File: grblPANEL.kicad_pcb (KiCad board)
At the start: 4 copper layers, 84 x 55 mm, 152 parts, among them J101 Conn_01x02, J201 2x5x1.27mm, J202 USB_C_Receptacle_USB2.0, J301 Conn_01x02, J401 Conn_01x02, J501 ILI9488, J601 Conn_02x10_Odd_Even, J701 Conn_01x04, J702 Conn_01x04, J703 Conn_01x04, J704 Conn_01x04, Q501 Q_NPN_BEC - S8050, SW201 SW_Push, SW202 SW_Push, U101 MAX17612A, U102 AZ1117-3.3, U201 STM32G0B1CxTxN, U202 USBLC6-2SC6, U301 SN65HVD230, U401 THVD1406, U601 ADP5589, Y201 8MHz

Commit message: some mcu..
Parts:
- removed TP101, TP102, TP103, TP104, TP105, TP301, TP302, TP303, TP304, TP401, TP402, TP403, TP404, TP501, TP502, TP503, TP504, TP505, TP506, TP507, TP601, TP602, TP701, TP702, TP703, TP704, TP705, TP706, TP707, TP708: TestPoint, TestPoint:TestPoint_THTPad_D2.0mm_Drill1.0mm
- moved R502 31.2 mm to (47.4, 170.4)
- moved R503 28.9 mm to (47.4, 168.7), turned to 0 degrees
- moved R603 15.1 mm to (54.8, 153.5), turned to 90 degrees
- moved R602 12.8 mm to (53.2, 153.5), turned to 90 degrees
- moved R601 10.7 mm to (51.6, 153.5), turned to 90 degrees
- moved R604 8.80 mm to (50.0, 153.5), turned to 90 degrees
- moved C206 5.94 mm to (28.2, 170.7)
- moved R201 5.59 mm to (25.5, 160.0), turned to -90 degrees
- moved R206 4.60 mm to (29.9, 170.7), turned to -90 degrees
- moved C203 3.31 mm to (31.5, 163.4), turned to -90 degrees
- moved C202 2.52 mm to (29.9, 163.4)
- moved C501 2.47 mm to (71.9, 148.3), turned to 90 degrees
- moved C204 2.40 mm to (44.9, 164.0)
- moved D201 2.40 mm to (39.9, 171.5)
- moved R203 2.40 mm to (47.4, 165.0)
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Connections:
- net Net-(J501-Pad11) renamed /Display/CONN_SCL
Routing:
- net DISPLAY_SDA: track 0.00 -> 34.5 mm
- net GND: track 49.0 -> 80.5 mm, vias 28 -> 50
- net DISPLAY_SDO: track 0.00 -> 28.1 mm
- net +3V3: track 35.7 -> 57.8 mm, vias 0 -> 1
- net DISPLAY_BACKLIGHT: track 0.00 -> 20.9 mm
- net DISPLAY_RESET: track 0.00 -> 15.1 mm
- net DISPLAY_CS: track 0.00 -> 14.3 mm
- net DISPLAY_D/C: track 0.00 -> 12.1 mm
- net /MCU/HSE_IN: track 0.00 -> 11.6 mm
- net /Display/CONN_SCL: track 0.00 -> 11.1 mm
- net /Display/DIO_GND: track 0.00 -> 10.0 mm
- net /MCU/CONN_SWDIO: track 0.00 -> 9.32 mm, vias 0 -> 1
- net /MCU/CONN_SWCLK: track 0.00 -> 8.90 mm, vias 0 -> 1
- net /MCU/CONN_~{RST}: track 0.00 -> 8.37 mm, vias 0 -> 1
- net /Keypad/KEYPAD_RST: track 0.00 -> 7.55 mm, vias 0 -> 2
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- added copper zone on F.Cu, net +3V3
- added copper zone on F.Cu, net GND

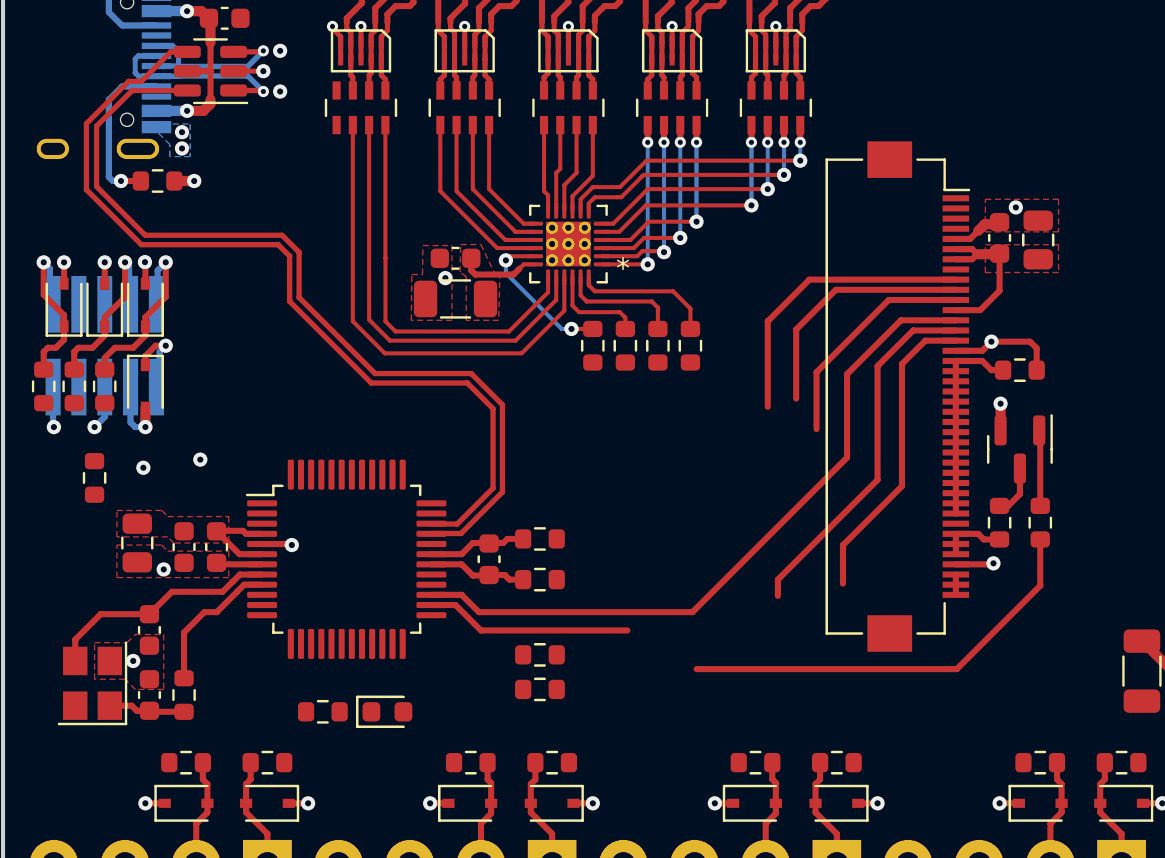
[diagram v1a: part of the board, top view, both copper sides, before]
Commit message: 1st crack at display routing
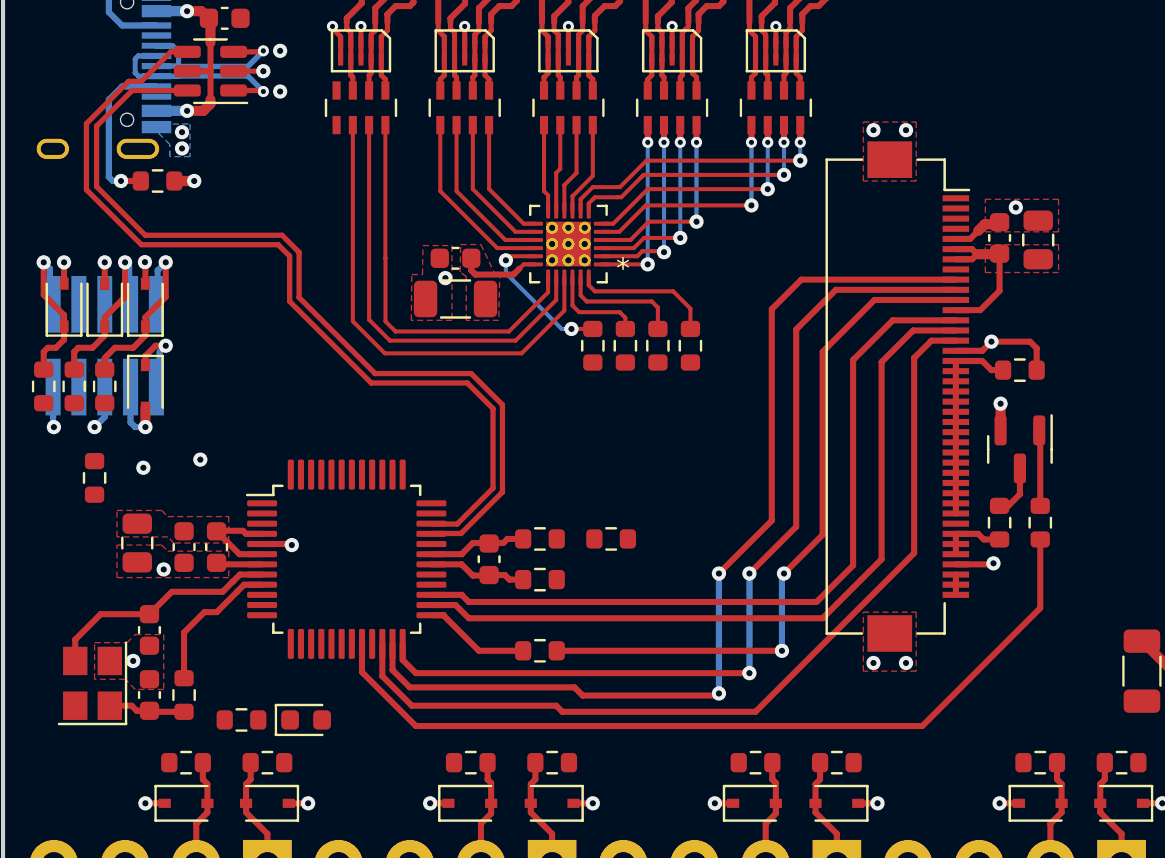
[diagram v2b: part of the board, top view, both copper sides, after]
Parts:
- moved R502 8.19 mm to (50.9, 163.0), turned to 0 degrees
- moved D201 4.02 mm to (35.9, 171.9)
- moved R205 4.02 mm to (32.7, 171.9)
- moved R503 0.20 mm to (47.4, 168.5)
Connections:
- J501 pad MP: (no net) -> GND
- U201 pad 23: DISPLAY_D/C -> DISPLAY_CS
- U201 pad 24: DISPLAY_CS -> DISPLAY_D/C
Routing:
- net DISPLAY_CS: track 14.3 -> 47.5 mm, vias 0 -> 2
- net DISPLAY_D/C: track 12.1 -> 44.6 mm, vias 0 -> 2
- net DISPLAY_RESET: track 15.1 -> 43.7 mm
- net /Display/CONN_SCL: track 11.1 -> 34.2 mm, vias 0 -> 2
- net DISPLAY_BACKLIGHT: track 20.9 -> 41.6 mm
- net DISPLAY_SDO: track 28.1 -> 37.6 mm
- net DISPLAY_SCL: track 0.00 -> 5.24 mm
- net DISPLAY_SDA: track 34.5 -> 37.6 mm
- net +3V3: track 57.8 -> 57.1 mm
- net GND: vias 50 -> 54
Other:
- board text removed: "ENCODER 3"

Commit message: modbus cleanup
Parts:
- moved C401 7.78 mm to (87.6, 144.3)
- moved R401 7.77 mm to (85.5, 151.7)
- moved R406 7.03 mm to (96.0, 151.5)
- moved R407 7.03 mm to (96.0, 144.5)
- moved R402 6.64 mm to (83.4, 144.3), turned to 180 degrees
- moved R403 6.11 mm to (91.0, 145.0)
- moved R404 6.06 mm to (92.7, 151.0)
- moved R405 6.06 mm to (92.7, 145.0)
- moved R201 5.20 mm to (30.7, 159.9), turned to 0 degrees
- moved R602 3.80 mm to (53.1, 157.3), turned to 180 degrees
- moved R604 3.29 mm to (53.1, 152.4), turned to 180 degrees
- moved R603 3.19 mm to (53.1, 150.8), turned to 180 degrees
- moved R601 2.66 mm to (53.1, 155.7), turned to 180 degrees
- moved D704 1.00 mm to (57.1, 175.4)
- moved D707 1.00 mm to (43.1, 175.4)
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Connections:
- D401 pad 1: /Modbus/CONN_RS485_A -> /Modbus/CONN_RS485_B
- D401 pad 2: /Modbus/CONN_RS485_B -> /Modbus/CONN_RS485_A
- J501 pad MP: GND -> (no net)
- JP401 pad 1: Net-(JP401-Pad1) -> /Modbus/RS485_A
- JP401 pad 2: /Modbus/RS485_B -> Net-(R403-Pad1)
- R403 pad 1: /Modbus/RS485_A -> Net-(R403-Pad1)
- R403 pad 2: Net-(JP401-Pad1) -> /Modbus/RS485_B
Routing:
- net /Modbus/RS485_A: track 36.9 -> 9.93 mm
- net KEYPAD_SDA: track 4.77 -> 27.5 mm, vias 0 -> 2
- net KEYPAD_CLK: track 5.97 -> 28.3 mm, vias 0 -> 2
- net MODBUS_RX: track 10.7 -> 1.98 mm
- net GND: track 80.5 -> 87.0 mm, vias 54 -> 60
- net /MCU/VREF+: track 1.48 -> 7.66 mm
- net /Keypad/KEYPAD_INT: track 6.85 -> 2.95 mm
- net Net-(R403-Pad1): track 0.00 -> 3.47 mm
- net /Encoders/CONN_ENC_2_B: track 5.28 -> 2.07 mm
- net /Modbus/CONN_RS485_B: track 9.33 -> 12.2 mm
- net /Modbus/CONN_RS485_A: track 9.35 -> 11.6 mm, vias 0 -> 1
- net /Keypad/KEYPAD_RST: track 7.55 -> 9.72 mm
- net Net-(JP401-Pad1): track 1.95 -> 0.00 mm
- net /Modbus/RS485_B: track 10.8 -> 9.19 mm
- net +3V3: track 57.1 -> 55.6 mm
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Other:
- board text added: "ENCODER 3"

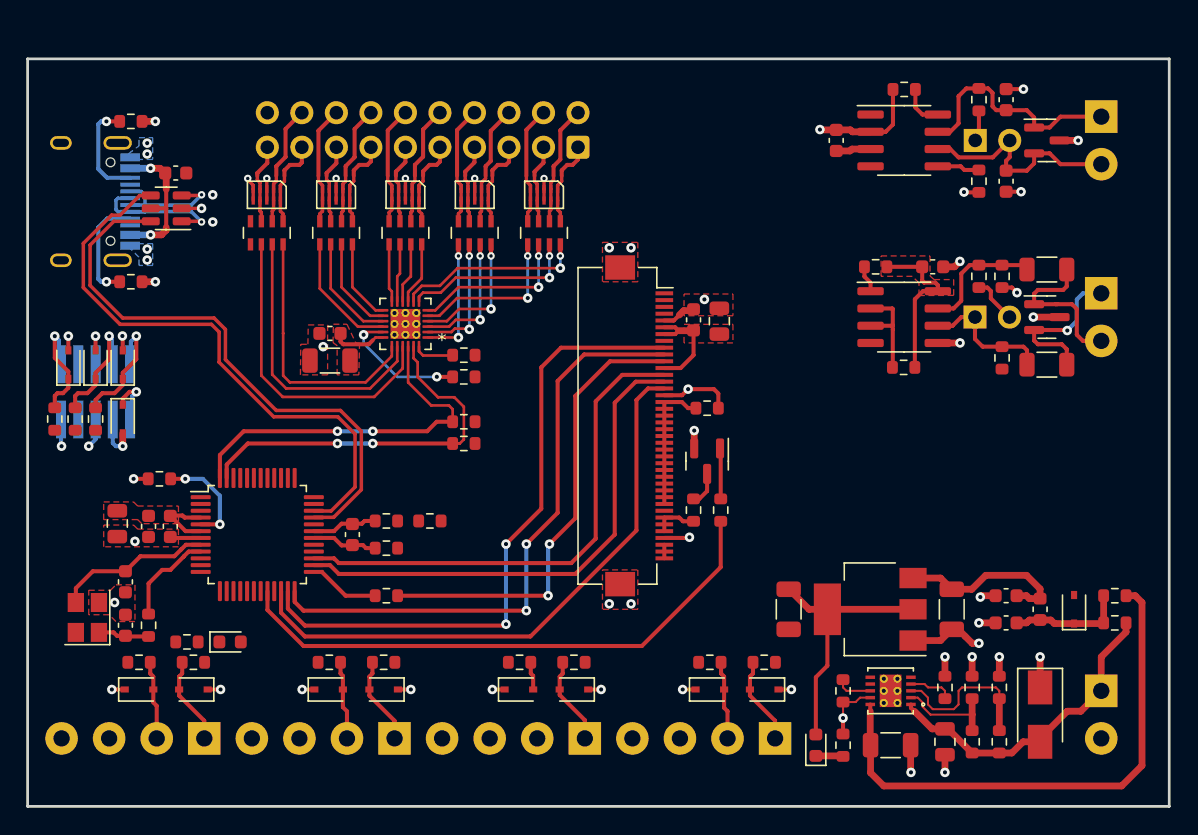
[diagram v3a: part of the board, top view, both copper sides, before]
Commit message: power section cleanup change 1206 caps to 0805
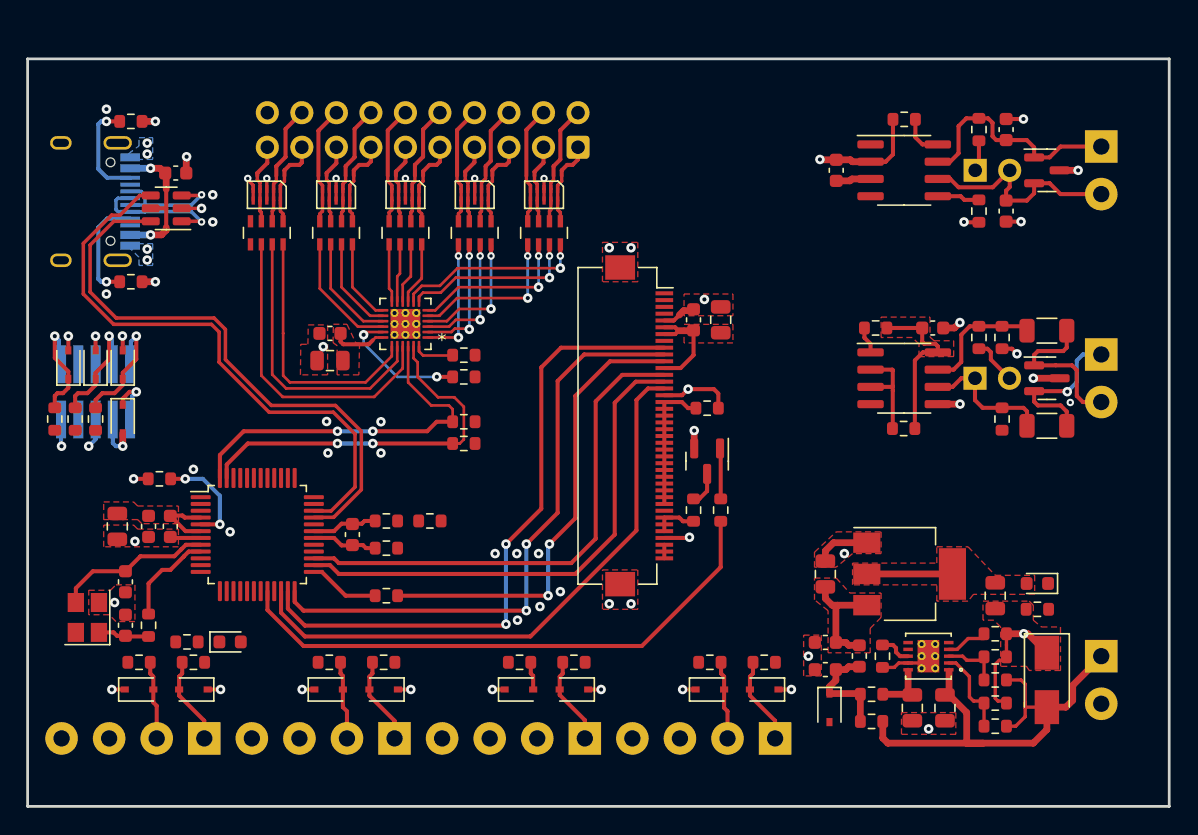
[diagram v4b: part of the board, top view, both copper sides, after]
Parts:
- C102, C105, C106, C601: footprint Capacitor_SMD:C_1206_3216Metric -> Capacitor_SMD:C_0805_2012Metric
- moved D103 20.2 mm to (95.3, 167.6), turned to 180 degrees
- moved D102 19.4 mm to (80.0, 176.8), turned to -90 degrees
- moved R107 19.3 mm to (83.1, 177.8)
- moved R108 19.3 mm to (83.1, 175.8)
- moved R109 17.4 mm to (95.3, 169.5), turned to 180 degrees
- moved C106 15.2 mm to (92.2, 168.5)
- moved C103 13.7 mm to (79.7, 173.9)
- moved C104 13.7 mm to (79.7, 171.9)
- moved L101 13.7 mm to (82.2, 172.9)
- moved C105 9.66 mm to (79.7, 166.9), turned to 90 degrees
- moved R105 5.41 mm to (92.2, 171.3), turned to 0 degrees
- moved R103 4.56 mm to (92.2, 174.7), turned to 180 degrees
- moved C401 4.50 mm to (87.6, 148.8)
- moved D401 4.50 mm to (96.0, 152.5)
- moved J401 4.50 mm to (100.0, 150.8)
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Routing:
- net /Power/VIN_PROT: track 39.4 -> 3.91 mm
- net VIN: track 23.0 -> 36.3 mm
- net +3V3: track 55.6 -> 42.6 mm
- net /Power/OVLO: track 11.6 -> 4.12 mm
- net /Power/VIN_PI_OUT: track 13.1 -> 8.71 mm
- net GND: track 87.0 -> 83.6 mm, vias 60 -> 70
- net /Power/PWR_LED_K: track 1.96 -> 0.00 mm
- net /Power/ULVO: track 7.56 -> 6.33 mm
- added copper zone on F.Cu, net /Power/VIN_PI_OUT
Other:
- board text added: "CAN TERMINATION"
- board text added: "DC POWER IN"
- board text added: "RS485 TERMINATION"
- board text added: "Vcc"
- board text removed: "3.3v"
- board text removed: "CAN TERM"
- board text removed: "RS485 TERM"

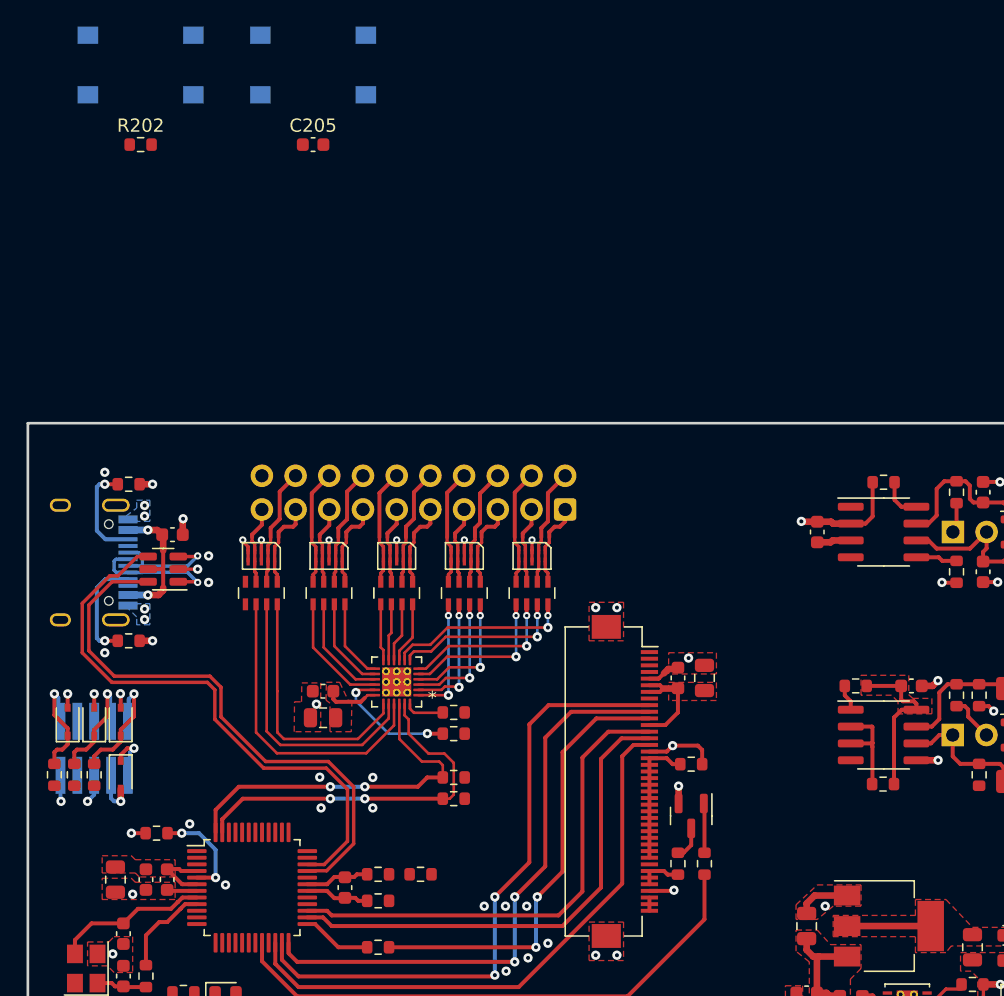
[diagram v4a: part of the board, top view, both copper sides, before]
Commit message: reset & bootloader buttons
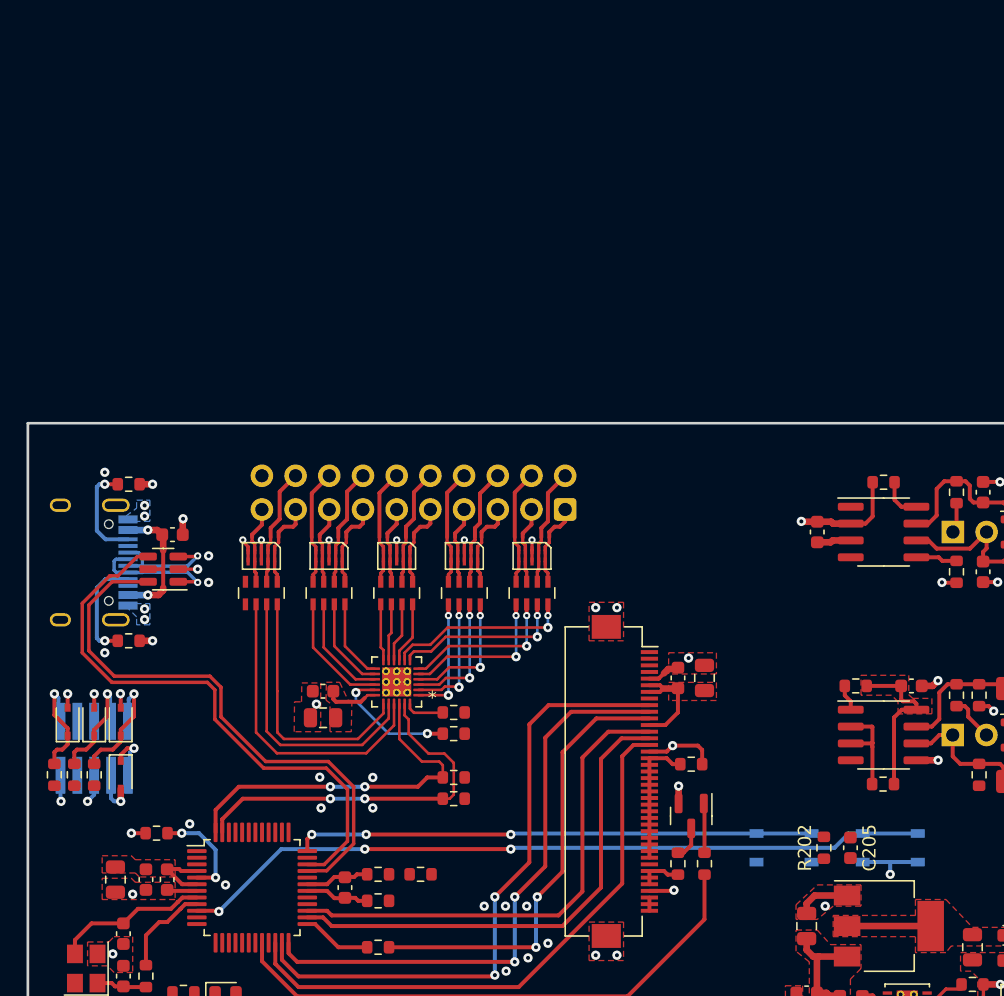
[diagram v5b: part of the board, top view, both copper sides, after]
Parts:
- SW201, SW202: footprint Button_Switch_SMD:SW_Push_1P1T_NO_6x6mm_H9.5mm -> Button_Switch_SMD:SW_SPST_PTS810
- moved SW201 76.4 mm to (78.0, 161.0)
- moved R202 73.9 mm to (81.0, 161.0), turned to 90 degrees
- moved SW202 73.3 mm to (86.0, 161.0)
- moved C205 66.7 mm to (83.0, 161.0), turned to -90 degrees
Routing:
- net /MCU/~{RST}: track 0.00 -> 56.8 mm, vias 0 -> 3
- net /MCU/SWCLK/BOOT0: track 0.00 -> 39.1 mm, vias 0 -> 3
- net GND: track 83.6 -> 88.7 mm, vias 70 -> 71
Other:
- board text added: "BOOT"
- board text added: "RESET"

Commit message: more routing
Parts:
- moved R205 66.3 mm to (98.8, 166.0), turned to -90 degrees
- moved D201 65.4 mm to (101.0, 166.0), turned to 90 degrees
- moved R109 9.19 mm to (98.8, 161.0), turned to -90 degrees
- moved D103 8.72 mm to (101.0, 161.0), turned to -90 degrees
- moved R602 3.20 mm to (50.0, 156.5)
- moved R601 3.20 mm to (50.0, 154.9)
- moved D701 1.20 mm to (75.2, 176.6)
- moved D702 1.20 mm to (61.2, 176.6)
- moved D703 1.20 mm to (71.2, 176.6)
- moved D704 1.20 mm to (57.1, 176.6)
- moved D705 1.20 mm to (47.2, 176.6)
- moved D706 1.20 mm to (33.2, 176.6)
- moved D707 1.20 mm to (43.1, 176.6)
- moved D708 1.20 mm to (29.2, 176.6)
- moved R701 1.20 mm to (75.2, 174.6)
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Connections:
- U201 pad 11: ENCODER_2_A -> ENCODER_4_A
- U201 pad 12: ENCODER_2_B -> ENCODER_4_B
- U201 pad 45: ENCODER_4_A -> ENCODER_2_A
- U201 pad 46: ENCODER_4_B -> ENCODER_2_B
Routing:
- net /MCU/LED: track 0.00 -> 92.4 mm
- net MODBUS_TX: track 0.00 -> 71.0 mm, vias 0 -> 2
- net MODBUS_RX: track 1.98 -> 65.9 mm, vias 0 -> 2
- net CAN_TX: track 0.00 -> 60.6 mm, vias 0 -> 2
- net CAN_RX: track 0.00 -> 57.0 mm, vias 0 -> 2
- net ENCODER_1_A: track 0.00 -> 40.2 mm, vias 0 -> 2
- net ENCODER_2_A: track 0.00 -> 38.1 mm, vias 0 -> 2
- net ENCODER_1_B: track 0.00 -> 36.1 mm, vias 0 -> 2
- net ENCODER_2_B: track 0.00 -> 31.2 mm, vias 0 -> 2
- net ENCODER_3_A: track 0.00 -> 18.4 mm, vias 0 -> 2
- net ENCODER_4_B: track 0.00 -> 13.6 mm, vias 0 -> 2
- net ENCODER_4_A: track 0.00 -> 11.8 mm, vias 0 -> 2
- net ENCODER_3_B: track 0.00 -> 9.26 mm
- net KEYPAD_SDA: track 27.5 -> 21.9 mm
- net KEYPAD_CLK: track 28.3 -> 22.7 mm
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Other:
- board text added: "Display panel: 83.98 x 54.53mm Edge cuts: 84.00 x 55.00mm"

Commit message: bit more routing buttons etc
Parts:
- moved R202 14.5 mm to (95.5, 161.8), turned to -90 degrees
- moved C205 13.6 mm to (95.5, 166.3)
- moved SW201 12.6 mm to (90.6, 161.8)
- moved SW202 7.02 mm to (90.6, 166.3)
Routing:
- net /MCU/SWCLK/BOOT0: track 39.1 -> 52.1 mm, vias 3 -> 5
- net /MCU/~{RST}: track 56.8 -> 67.1 mm, vias 3 -> 6
- net Net-(R202-Pad1): track 0.00 -> 8.46 mm, vias 0 -> 1
- net GND: track 91.5 -> 93.5 mm
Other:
- board text added: "PWR"
- board text added: "USR"
